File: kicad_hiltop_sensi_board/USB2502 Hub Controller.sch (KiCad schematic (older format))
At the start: 49 parts, among them U27 USB2502, U7 DNF, Y1 50ppm 24.000MHZ

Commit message: revb design updated schematics and layout
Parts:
- removed D1: B240A-13, Diode_SMD:D_SMA, symbol device:D_Schottky
- C91: value 1.0uF -> 1uF
- R102: value 10K -> 20K
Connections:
- net +5V: now also C91.1, C92.1, R99.1
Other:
- moved on the sheet: R99
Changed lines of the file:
@@
 Connection ~ 8700 7500
-$Comp
-L device:D_Schottky D1
-U 1 1 5DC9FCDD
-P 4650 2050
-F 0 "D1" H 4650 2266 50  0000 C CNN
-F 1 "B240A-13" H 4650 2175 50  0000 C CNN
-F 2 "Diode_SMD:D_SMA" H 4650 2050 50  0001 C CNN
-F 3 "" H 4650 2050 50  0001 C CNN
-F 4 "133-008" H 4650 2050 50  0001 C CNN "Devtank"
-	1    4650 2050
-	1    0    0    -1
-$EndComp
 $Comp
 L device:C C91
 U 1 1 5DCA03F2
 P 5250 2200
-F 0 "C91" H 4995 2160 50  0000 L CNN
-F 1 "1.0uF " H 4990 2080 50  0000 L CNN
+F 0 "C91" H 5000 2250 50  0000 L CNN
+F 1 "1uF " H 5000 2175 50  0000 L CNN
 F 2 "Capacitor_SMD:C_0402_1005Metric" H 5288 2050 50  0001 C CNN
 F 3 "" H 5250 2200 50  0001 C CNN
@@
 Wire Wire Line
 	4300 1900 4300 2050
-Wire Wire Line
-	4300 2050 4500 2050
 Connection ~ 5250 2050
 $Comp
 L device:R R99
 U 1 1 5DD02F8D
-P 4900 2250
-F 0 "R99" H 4695 2310 50  0000 L CNN
-F 1 "10K" H 4690 2230 50  0000 L CNN
-F 2 "Resistor_SMD:R_0603_1608Metric" V 4830 2250 50  0001 C CNN
-F 3 "" H 4900 2250 50  0001 C CNN
-F 4 "101-010" H 4900 2250 50  0001 C CNN "Devtank"
-	1    4900 2250
+P 4900 2475
+F 0 "R99" H 4695 2535 50  0000 L CNN
+F 1 "10K" H 4690 2455 50  0000 L CNN
+F 2 "Resistor_SMD:R_0603_1608Metric" V 4830 2475 50  0001 C CNN
+F 3 "" H 4900 2475 50  0001 C CNN
+F 4 "101-010" H 4900 2475 50  0001 C CNN "Devtank"
+	1    4900 2475
 	1    0    0    -1
 $EndComp
@@
 U 1 1 5DD0335D
 P 4900 3200
-F 0 "R102" H 4970 3246 50  0000 L CNN
-F 1 "10K" H 4970 3155 50  0000 L CNN
+F 0 "R102" H 4650 3275 50  0000 L CNN
+F 1 "20K" H 4700 3175 50  0000 L CNN
 F 2 "Resistor_SMD:R_0603_1608Metric" V 4830 3200 50  0001 C CNN
 F 3 "" H 4900 3200 50  0001 C CNN
@@
 	4900 2850 5150 2850
 Wire Wire Line
-	4800 2050 4900 2050
-Wire Wire Line
 	4900 2850 4900 3050
 Wire Wire Line
-	4900 2100 4900 2050
+	4900 2325 4900 2050
 Connection ~ 4900 2050
 Wire Wire Line
@@
 USBDN2
 Wire Wire Line
-	4900 2400 4900 2850
+	4900 2625 4900 2850
 Connection ~ 4900 2850
 $Comp
@@
 Wire Wire Line
 	9115 3715 9115 3965
+Wire Wire Line
+	4300 2050 4900 2050
 $EndSCHEMATC

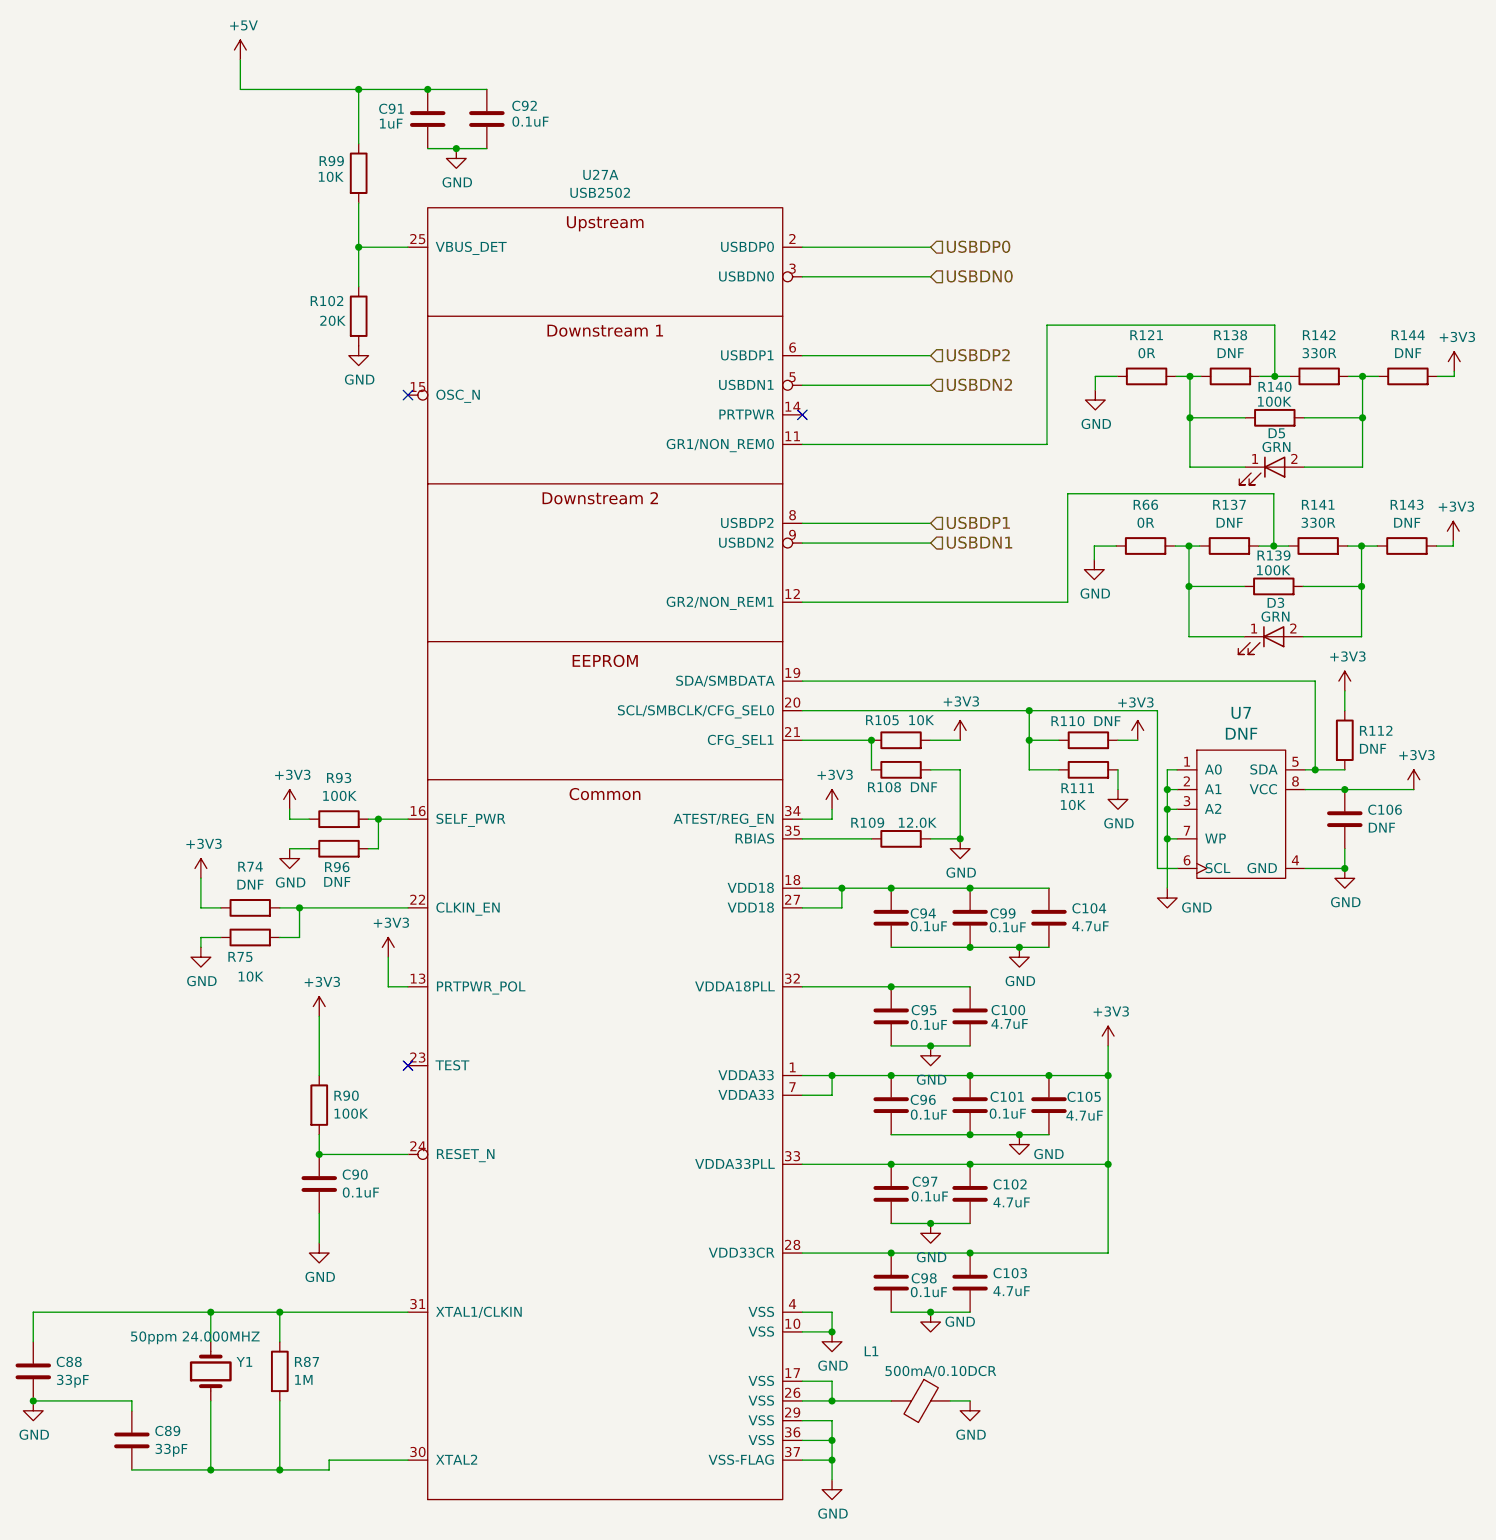
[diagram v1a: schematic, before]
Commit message: updated footprints to simplify bom
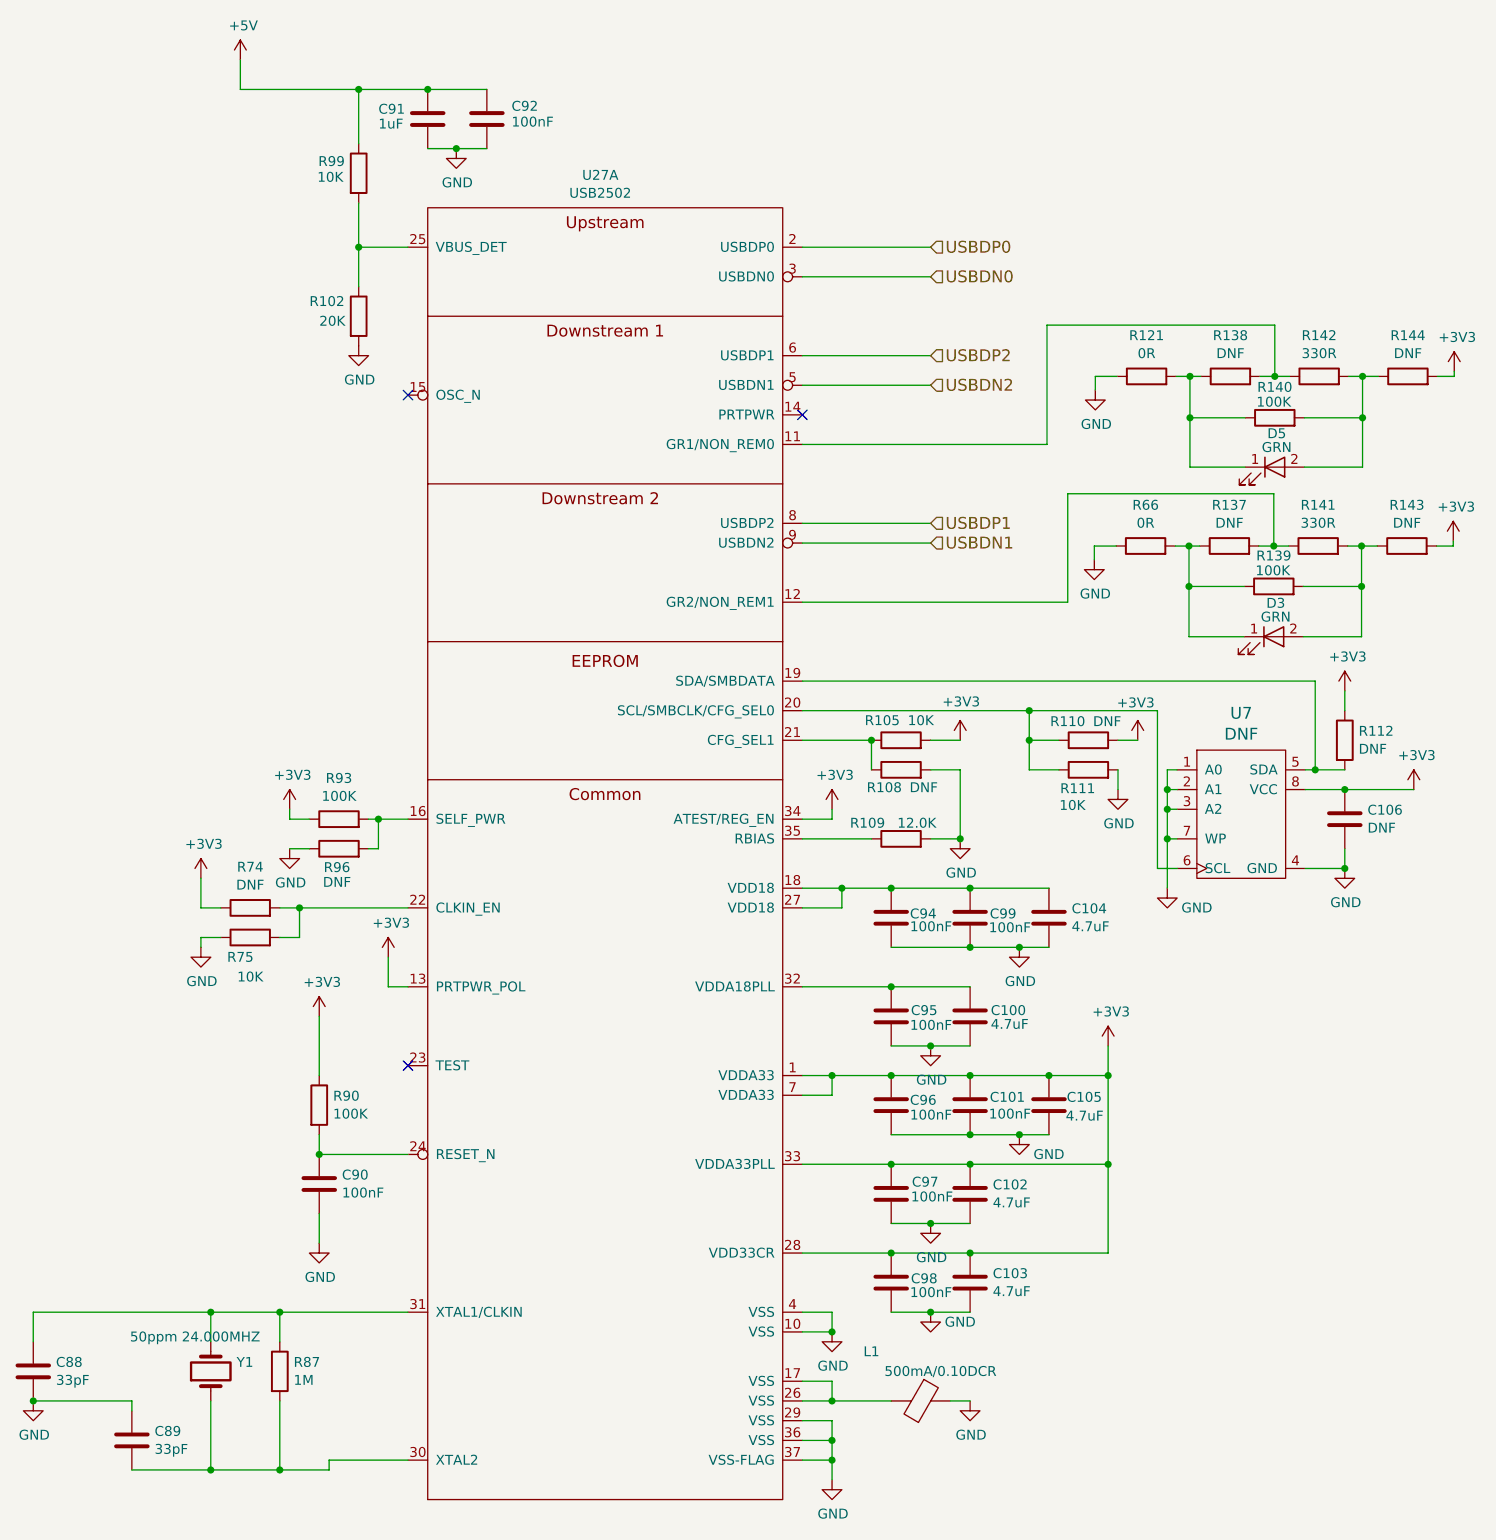
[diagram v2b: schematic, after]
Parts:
- C100, C103, C105: value 4.7uF -> 4.7uF
- C101, C90, C92, C94, C95, C96, C97, C98, C99: value 0.1uF -> 100nF
- R75: value 10K -> 10K
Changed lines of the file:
@@
 P 8000 7200
 F 0 "C101" H 8100 7240 50  0000 L CNN
-F 1 "0.1uF" H 8095 7155 50  0000 L CNN
+F 1 "100nF" H 8095 7155 50  0000 L CNN
 F 2 "Capacitor_SMD:C_0402_1005Metric" H 8038 7050 50  0001 C CNN
 F 3 "" H 8000 7200 50  0001 C CNN
@@
 P 8400 7200
 F 0 "C105" H 8490 7240 50  0000 L CNN
-F 1 "4.7uF " H 8485 7145 50  0000 L CNN
+F 1 "4.7uF" H 8485 7145 50  0000 L CNN
 F 2 "Capacitor_SMD:C_0402_1005Metric" H 8438 7050 50  0001 C CNN
 F 3 "" H 8400 7200 50  0001 C CNN
@@
 P 7600 7200
 F 0 "C96" H 7695 7225 50  0000 L CNN
-F 1 "0.1uF" H 7695 7150 50  0000 L CNN
+F 1 "100nF" H 7695 7150 50  0000 L CNN
 F 2 "Capacitor_SMD:C_0402_1005Metric" H 7638 7050 50  0001 C CNN
 F 3 "" H 7600 7200 50  0001 C CNN
@@
 P 7600 7650
 F 0 "C97" H 7705 7710 50  0000 L CNN
-F 1 "0.1uF" H 7700 7635 50  0000 L CNN
+F 1 "100nF" H 7700 7635 50  0000 L CNN
 F 2 "Capacitor_SMD:C_0402_1005Metric" H 7638 7500 50  0001 C CNN
 F 3 "" H 7600 7650 50  0001 C CNN
@@
 P 7600 6750
 F 0 "C95" H 7700 6780 50  0000 L CNN
-F 1 "0.1uF" H 7695 6705 50  0000 L CNN
+F 1 "100nF" H 7695 6705 50  0000 L CNN
 F 2 "Capacitor_SMD:C_0402_1005Metric" H 7638 6600 50  0001 C CNN
 F 3 "" H 7600 6750 50  0001 C CNN
@@
 P 8000 6750
 F 0 "C100" H 8105 6780 50  0000 L CNN
-F 1 "4.7uF " H 8105 6710 50  0000 L CNN
+F 1 "4.7uF" H 8105 6710 50  0000 L CNN
 F 2 "Capacitor_SMD:C_0402_1005Metric" H 8038 6600 50  0001 C CNN
 F 3 "" H 8000 6750 50  0001 C CNN
@@
 P 8000 6250
 F 0 "C99" H 8100 6270 50  0000 L CNN
-F 1 "0.1uF" H 8095 6200 50  0000 L CNN
+F 1 "100nF" H 8095 6200 50  0000 L CNN
 F 2 "Capacitor_SMD:C_0402_1005Metric" H 8038 6100 50  0001 C CNN
 F 3 "" H 8000 6250 50  0001 C CNN
@@
 P 7600 6250
 F 0 "C94" H 7695 6270 50  0000 L CNN
-F 1 "0.1uF" H 7695 6205 50  0000 L CNN
+F 1 "100nF" H 7695 6205 50  0000 L CNN
 F 2 "Capacitor_SMD:C_0402_1005Metric" H 7638 6100 50  0001 C CNN
 F 3 "" H 7600 6250 50  0001 C CNN
@@
 P 4350 6350
 F 0 "R75" V 4250 6400 50  0000 C CNN
-F 1 "10K " V 4150 6350 50  0000 C CNN
+F 1 "10K" V 4150 6350 50  0000 C CNN
 F 2 "Resistor_SMD:R_0603_1608Metric" V 4280 6350 50  0001 C CNN
 F 3 "" H 4350 6350 50  0001 C CNN
@@
 P 4700 7600
 F 0 "C90" H 4815 7646 50  0000 L CNN
-F 1 "0.1uF" H 4815 7555 50  0000 L CNN
+F 1 "100nF" H 4815 7555 50  0000 L CNN
 F 2 "Capacitor_SMD:C_0603_1608Metric" H 4738 7450 50  0001 C CNN
 F 3 "" H 4700 7600 50  0001 C CNN
@@
 P 8000 8100
 F 0 "C103" H 8115 8146 50  0000 L CNN
-F 1 "4.7uF " H 8115 8055 50  0000 L CNN
+F 1 "4.7uF" H 8115 8055 50  0000 L CNN
 F 2 "Capacitor_SMD:C_0402_1005Metric" H 8038 7950 50  0001 C CNN
 F 3 "" H 8000 8100 50  0001 C CNN
@@
 P 7600 8100
 F 0 "C98" H 7700 8120 50  0000 L CNN
-F 1 "0.1uF" H 7695 8050 50  0000 L CNN
+F 1 "100nF" H 7695 8050 50  0000 L CNN
 F 2 "Capacitor_SMD:C_0402_1005Metric" H 7638 7950 50  0001 C CNN
 F 3 "" H 7600 8100 50  0001 C CNN
@@
 P 5550 2200
 F 0 "C92" H 5675 2265 50  0000 L CNN
-F 1 "0.1uF" H 5675 2185 50  0000 L CNN
+F 1 "100nF" H 5675 2185 50  0000 L CNN
 F 2 "Capacitor_SMD:C_0402_1005Metric" H 5588 2050 50  0001 C CNN
 F 3 "" H 5550 2200 50  0001 C CNN
